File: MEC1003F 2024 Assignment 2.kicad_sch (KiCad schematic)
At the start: 16 parts, among them U1 AP331AWRG-7, U2 AP331AWRG-7

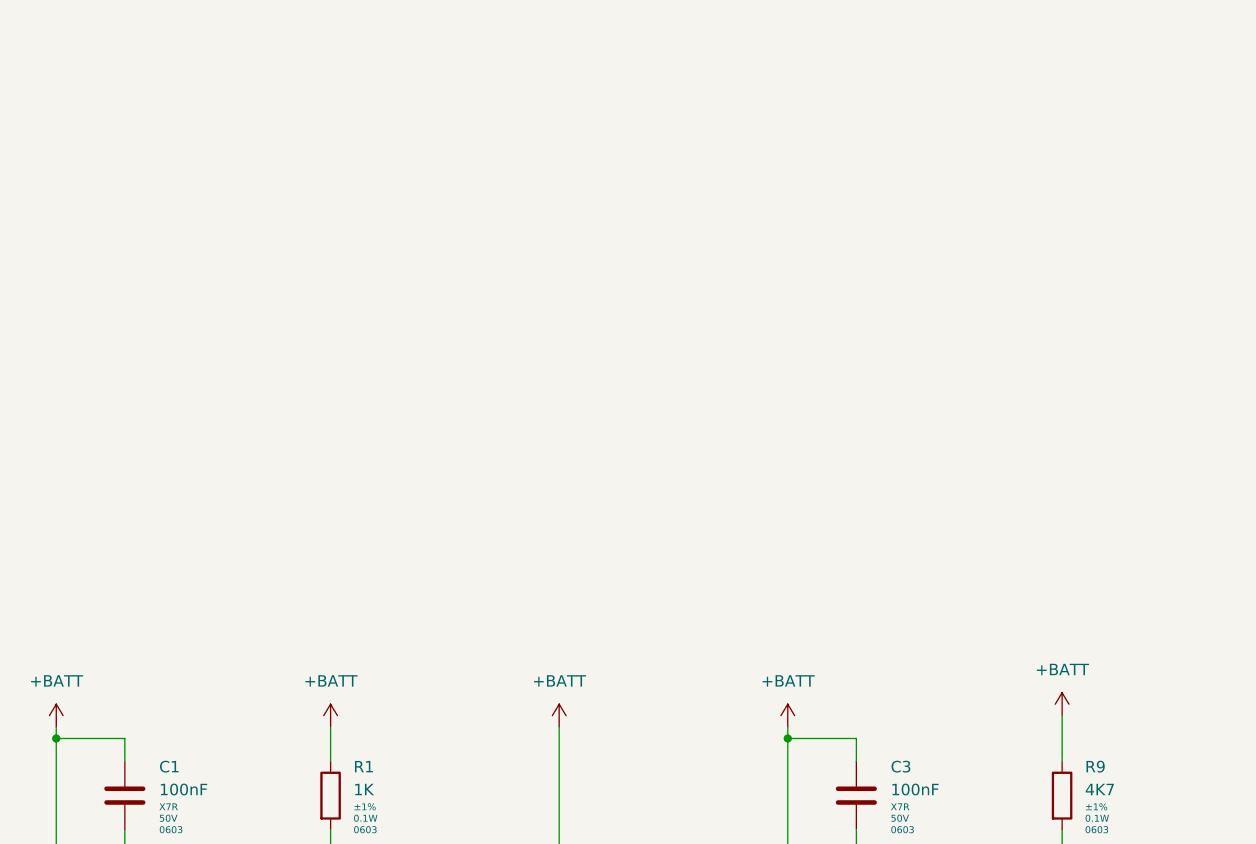
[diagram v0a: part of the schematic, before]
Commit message: Rename Project & Add Voltage Regulator + Footprints
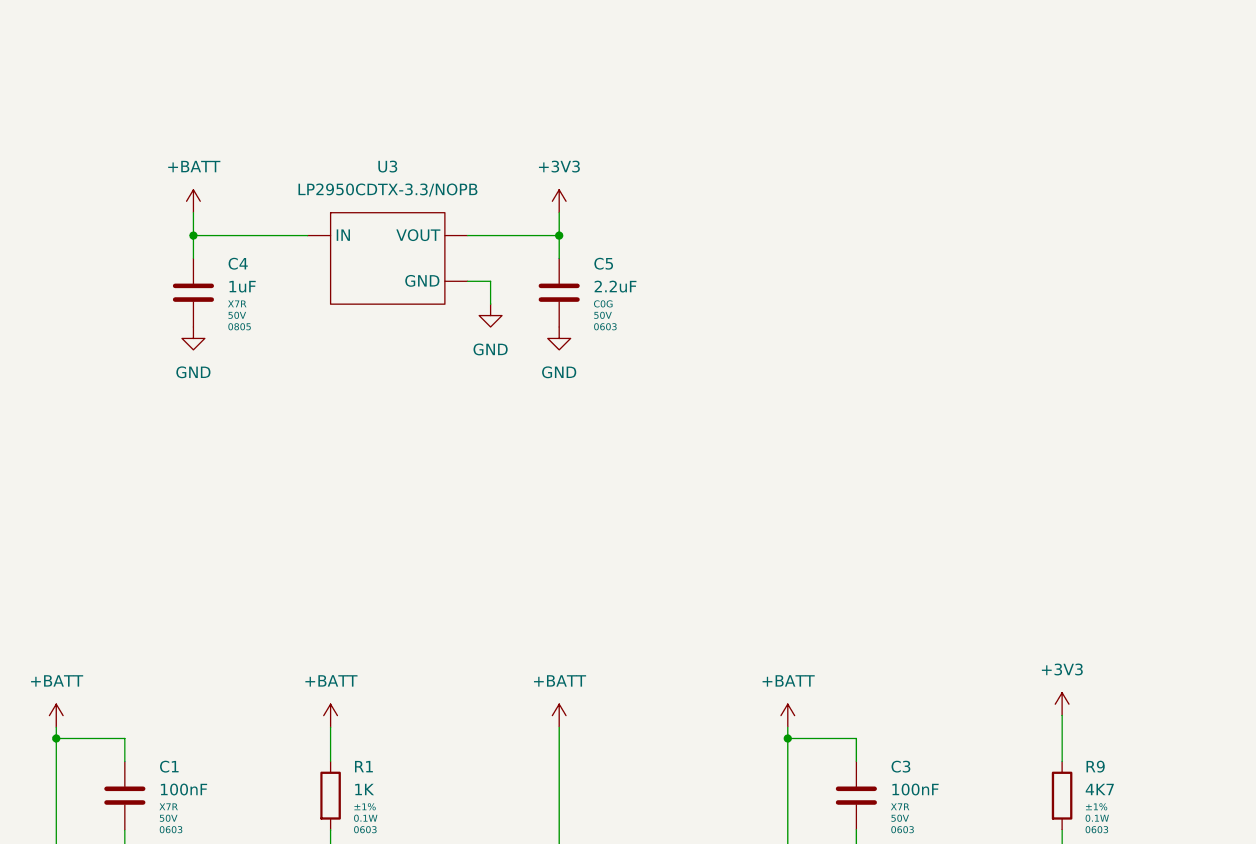
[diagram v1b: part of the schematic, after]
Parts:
- added C4: 1uF, Capacitor_SMD:C_0805_2012Metric, symbol Project Symbols:CL21B105KBFNNNE
- added C5: 2.2uF, Capacitor_SMD:C_1206_3216Metric, symbol Project Symbols:CL31B225KBHNNNE
- added U3: LP2950CDTX-3.3/NOPB, symbol Project Symbols:LP2950CDTX-3.3/NOPB
- J1, J2: footprint (none) -> Project Footprints:CROC MEDIUM
- R1, R3, R4, R5, R6, R7, R8: footprint (none) -> Resistor_SMD:R_0603_1608Metric
- U1, U2: footprint (none) -> Project Footprints:SOT-23-5 (AP331A) MRF
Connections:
- net +BATT: now also C4.1, U3. (VOUT); no longer R9.1
- net GND: now also C4.2, C5.2, U3. (VOUT)
- new net +3V3: C5.1, R9.1, U3. (VOUT)
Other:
- title: MEC1003F 2024 Lecture 2 Demo -> MEC1003F 2024 Assignment 2
